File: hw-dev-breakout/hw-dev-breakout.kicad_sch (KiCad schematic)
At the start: 5 parts, among them J1 CN7, J2 CN10

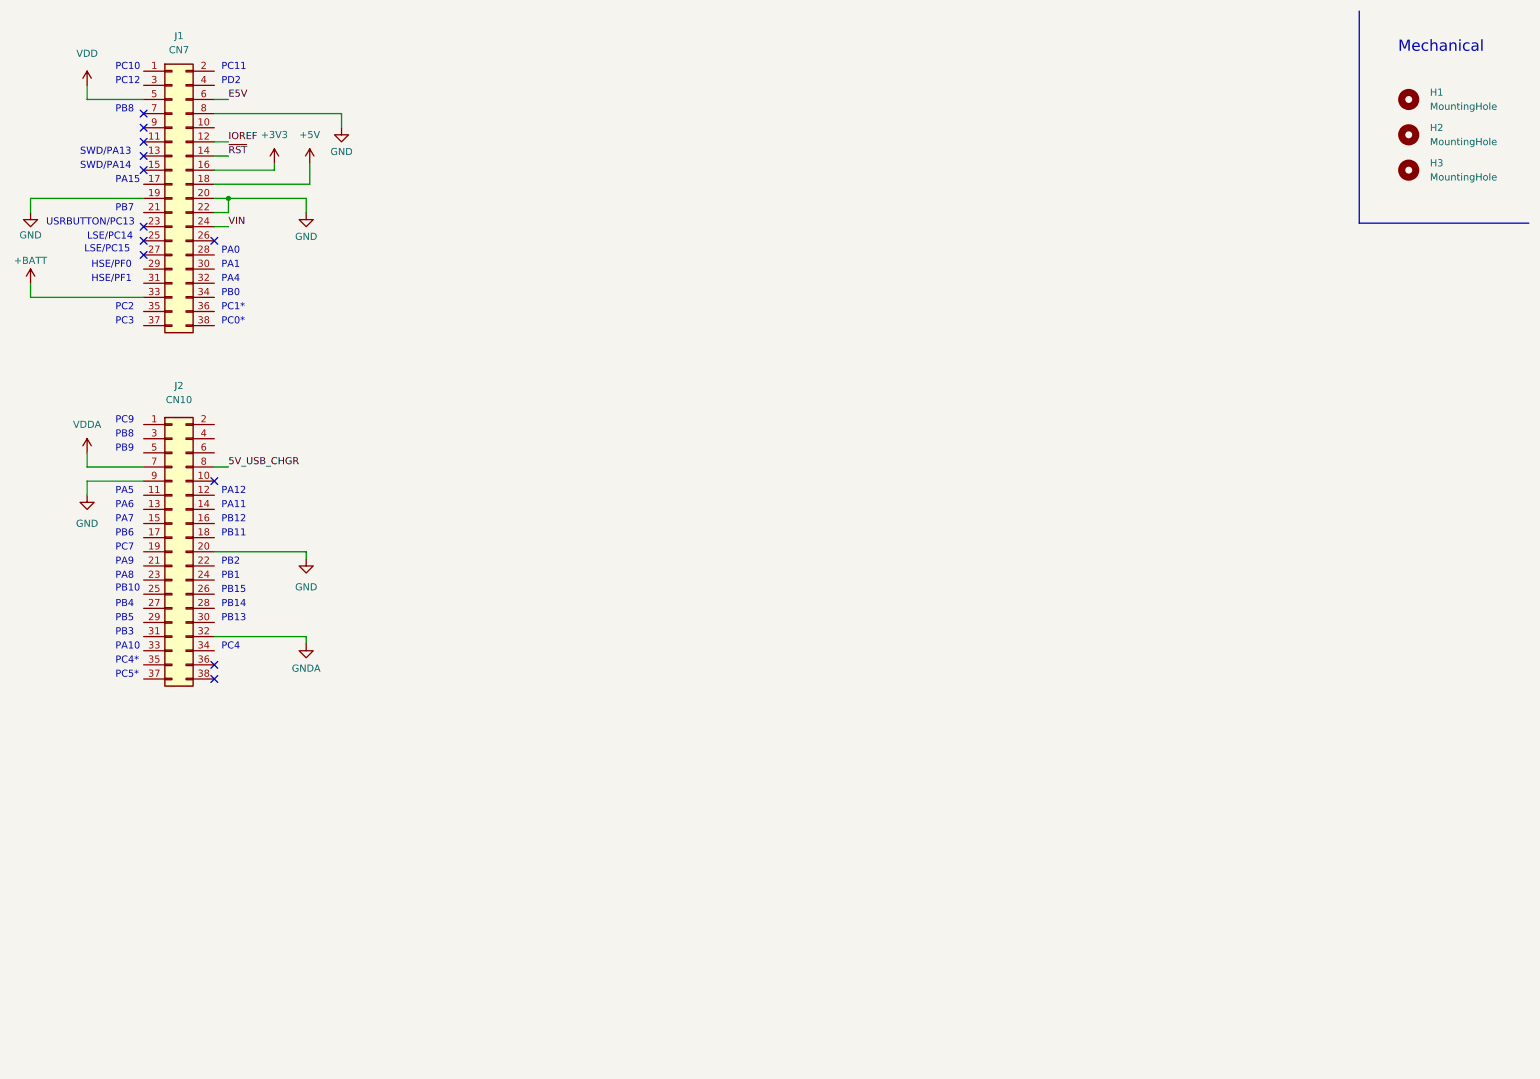
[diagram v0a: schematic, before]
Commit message: WIP: Active level shifting, too many components
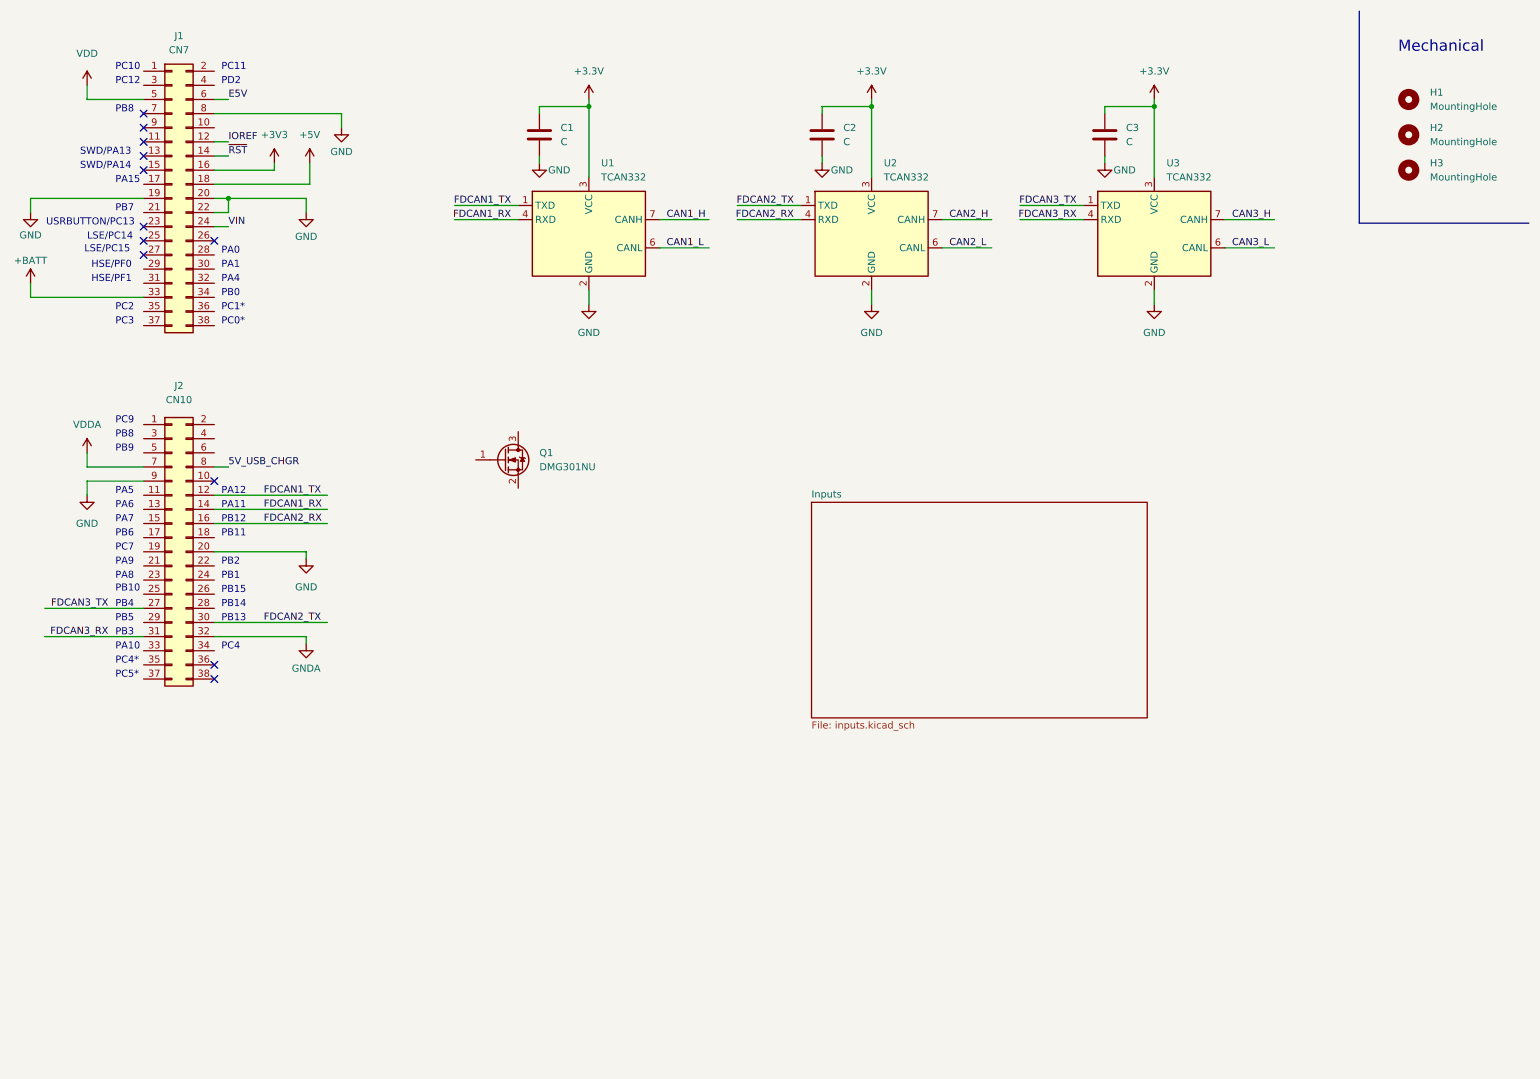
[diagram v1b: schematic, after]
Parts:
- added C1, C2, C3: C, symbol Device:C
- added Q1: DMG301NU, Package_TO_SOT_SMD:SOT-23, symbol Device:Q_NMOS_GSD
- added U1, U2, U3: TCAN332, symbol Interface_CAN_LIN:TCAN332
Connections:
- net GND: now also C1.2, C2.2, C3.2, U1.2 (GND), U2.2 (GND), U3.2 (GND)
- net FDCAN1_TX: now reaches J2.12 (Pin_12)
- net FDCAN1_TX: now also U1.1 (TXD)
- net FDCAN1_RX: now reaches J2.14 (Pin_14)
- net FDCAN1_RX: now also U1.4 (RXD)
- net FDCAN2_RX: now reaches J2.16 (Pin_16)
- net FDCAN2_RX: now also U2.4 (RXD)
- net FDCAN3_TX: now reaches J2.27 (Pin_27)
- net FDCAN3_TX: now also U3.1 (TXD)
- net FDCAN2_TX: now reaches J2.30 (Pin_30)
- net FDCAN2_TX: now also U2.1 (TXD)
- net FDCAN3_RX: now reaches J2.31 (Pin_31)
- net FDCAN3_RX: now also U3.4 (RXD)
- new net +3.3V: C1.1, C2.1, C3.1, U1.3 (VCC), U2.3 (VCC), U3.3 (VCC)
- new net CAN1_H: U1.7 (CANH)
- new net CAN1_L: U1.6 (CANL)
- new net CAN2_H: U2.7 (CANH)
- new net CAN2_L: U2.6 (CANL)
- new net CAN3_H: U3.7 (CANH)
- new net CAN3_L: U3.6 (CANL)
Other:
- added sheet Inputs (inputs.kicad_sch)

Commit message: Schematic mostly done, pre-resistor pack swap
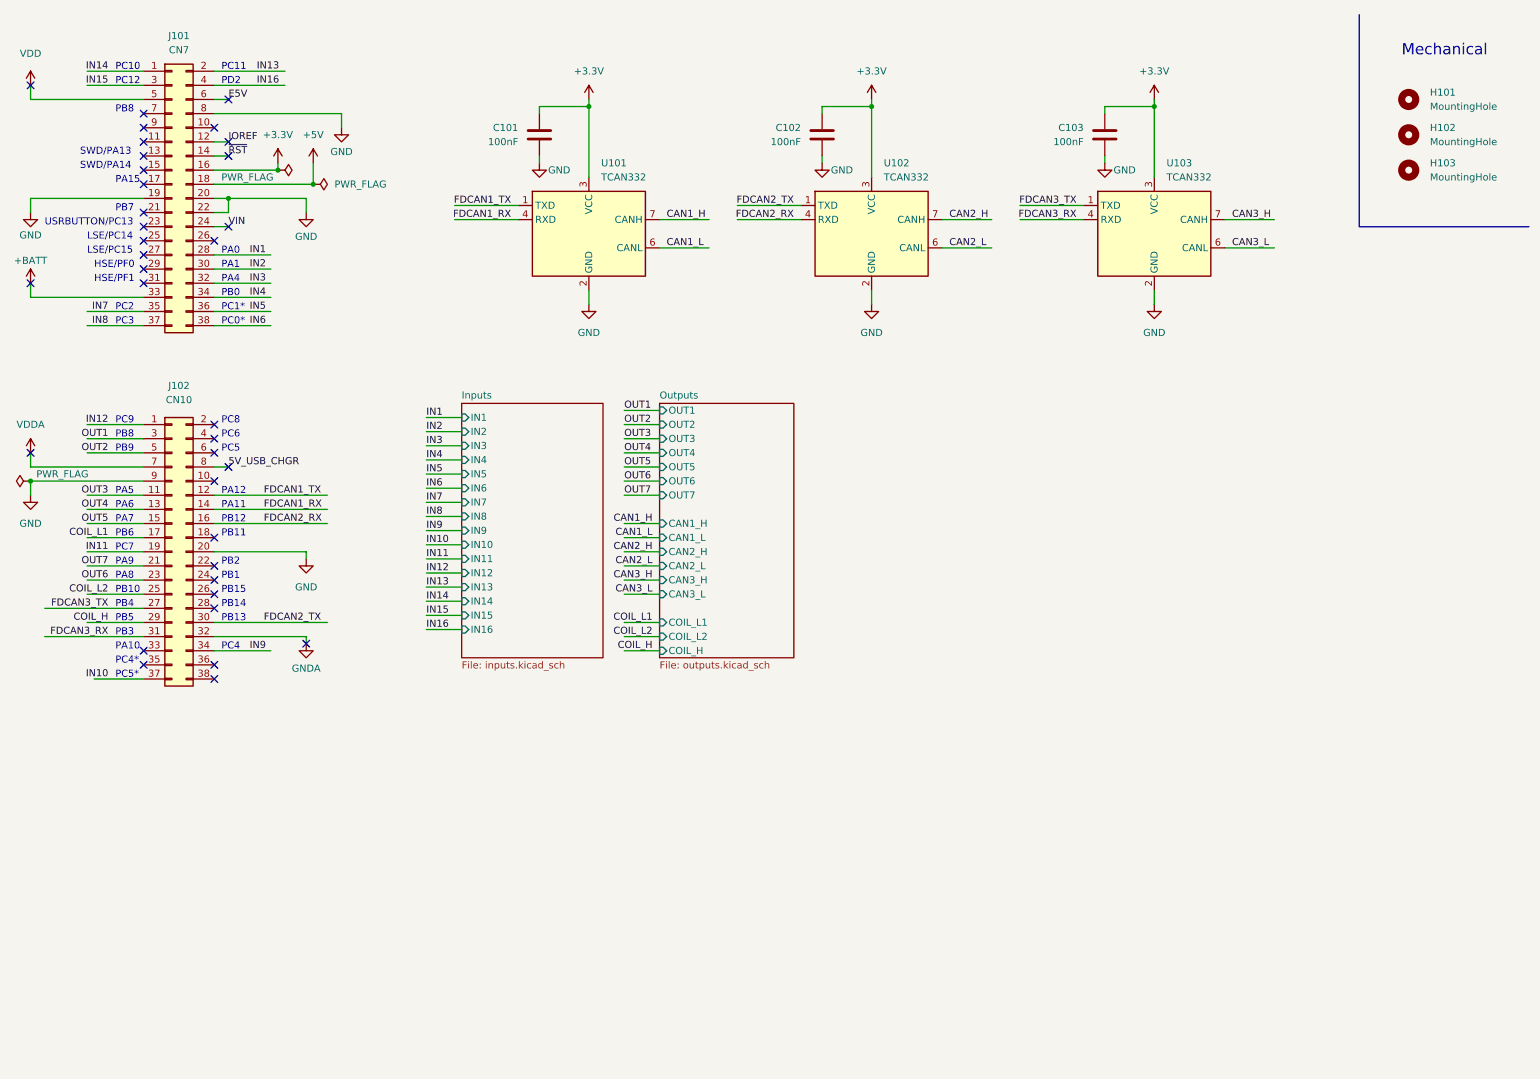
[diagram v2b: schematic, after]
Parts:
- removed Q1: DMG301NU, Package_TO_SOT_SMD:SOT-23, symbol Device:Q_NMOS_GSD
- C101: renamed from C1; value C -> 100nF; footprint (none) -> Capacitor_SMD:C_0603_1608Metric
- C102: renamed from C2; value C -> 100nF; footprint (none) -> Capacitor_SMD:C_0603_1608Metric
- C103: renamed from C3; value C -> 100nF; footprint (none) -> Capacitor_SMD:C_0603_1608Metric
- U101: renamed from U1; footprint (none) -> Package_SO:SOIC-8_3.9x4.9mm_P1.27mm
- U102: renamed from U2; footprint (none) -> Package_SO:SOIC-8_3.9x4.9mm_P1.27mm
- U103: renamed from U3; footprint (none) -> Package_SO:SOIC-8_3.9x4.9mm_P1.27mm
- renumbered H1 to H101, H2 to H102, H3 to H103, J1 to J101, J2 to J102
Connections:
- net +3V3 is gone; now on net +3.3V: J101.16 (Pin_16)
- net IN14: now reaches J101.1 (Pin_1)
- net IN13: now reaches J101.2 (Pin_2)
- net IN1: now reaches J101.28 (Pin_28)
- net IN15: now reaches J101.3 (Pin_3)
- net IN2: now reaches J101.30 (Pin_30)
- net IN3: now reaches J101.32 (Pin_32)
- net IN4: now reaches J101.34 (Pin_34)
- net IN7: now reaches J101.35 (Pin_35)
- net IN5: now reaches J101.36 (Pin_36)
- net IN8: now reaches J101.37 (Pin_37)
- net IN6: now reaches J101.38 (Pin_38)
- net IN16: now reaches J101.4 (Pin_4)
- net IN12: now reaches J102.1 (Pin_1)
- net OUT3: now reaches J102.11 (Pin_11)
- net OUT4: now reaches J102.13 (Pin_13)
- net OUT5: now reaches J102.15 (Pin_15)
- net COIL_L1: now reaches J102.17 (Pin_17)
- net IN11: now reaches J102.19 (Pin_19)
- net OUT7: now reaches J102.21 (Pin_21)
- net OUT6: now reaches J102.23 (Pin_23)
- net COIL_L2: now reaches J102.25 (Pin_25)
- net COIL_H: now reaches J102.29 (Pin_29)
- net OUT1: now reaches J102.3 (Pin_3)
- net IN9: now reaches J102.34 (Pin_34)
- net IN10: now reaches J102.37 (Pin_37)
- net OUT2: now reaches J102.5 (Pin_5)
- no-connect marks 12 -> 36
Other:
- added sheet Outputs (outputs.kicad_sch)
- sheet Inputs ports: added IN1, IN10, IN11, IN12, IN13, IN14, IN15, IN16, IN2, IN3, IN4, IN5, IN6, IN7, IN8, IN9; removed none
- note added: "PC5"
- note added: "PC6"
- note added: "PC8"

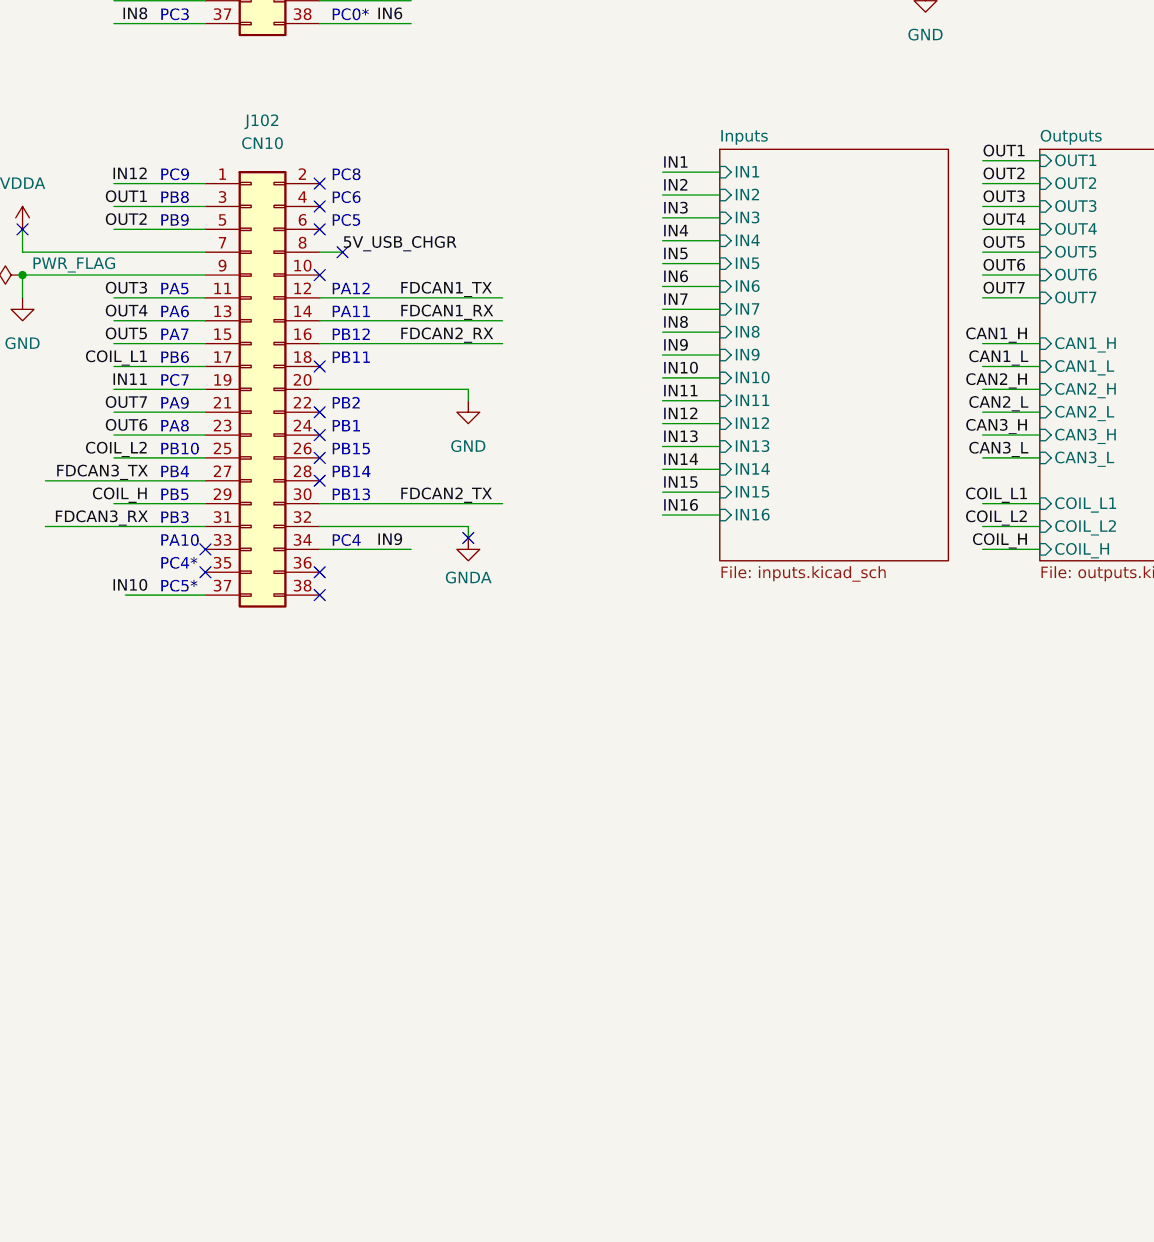
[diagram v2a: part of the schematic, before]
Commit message: Complete schematic with footprint assignments
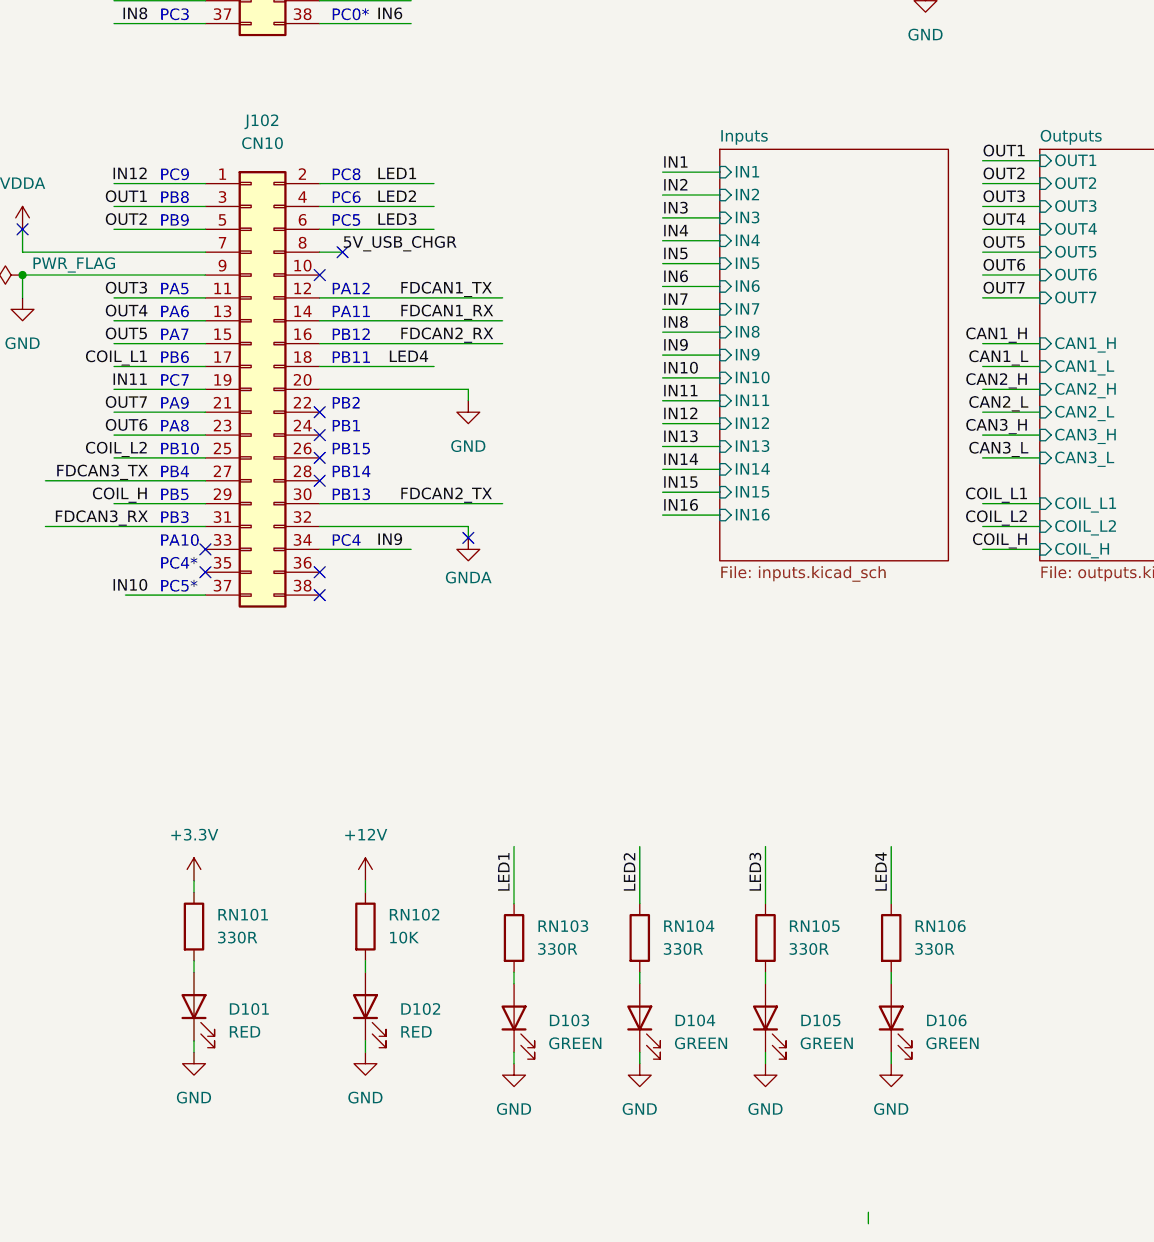
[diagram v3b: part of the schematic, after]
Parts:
- added D101, D102: RED, LED_SMD:LED_0603_1608Metric, symbol Device:LED
- added D103, D104, D105, D106: GREEN, LED_SMD:LED_0603_1608Metric, symbol Device:LED
- added RN101, RN103, RN104, RN105, RN106: 330R, Resistor_SMD:R_0603_1608Metric, symbol Device:R
- added RN102: 10K, Resistor_SMD:R_0603_1608Metric, symbol Device:R
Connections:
- net +3.3V: now also RN101.1
- net GND: now also D101.1 (K), D102.1 (K), D103.1 (K), D104.1 (K), D105.1 (K), D106.1 (K)
- net LED4: now reaches J102.18 (Pin_18)
- net LED4: now also RN106.1
- net LED1: now reaches J102.2 (Pin_2)
- net LED1: now also RN103.1
- net LED2: now reaches J102.4 (Pin_4)
- net LED2: now also RN104.1
- net LED3: now reaches J102.6 (Pin_6)
- net LED3: now also RN105.1
- new net: D103.2 (A), RN103.2
- new net: D104.2 (A), RN104.2
- new net: D105.2 (A), RN105.2
- new net: D101.2 (A), RN101.2
- new net: D106.2 (A), RN106.2
- new net: D102.2 (A), RN102.2
- new net +12V: RN102.1
- no-connect marks 36 -> 32

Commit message: pcb: Initial components placed
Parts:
- removed H101, H102, H103: MountingHole, MountingHole:MountingHole_3.2mm_M3, symbol Mechanical:MountingHole
- added SW101: SW_Push, Button_Switch_THT:SW_PUSH_6mm_H8mm, symbol Switch:SW_Push
- renumbered RN101 to R101, RN102 to R102, RN103 to R103, RN104 to R104, RN105 to R105, RN106 to R106
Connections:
- net GND: now also SW101.1
- net ~{RST}: now also SW101.2
- net +BATT: no longer names the net of J101.33 (Pin_33)
- net GNDA: no longer names the net of J102.32 (Pin_32)
- net VDD: no longer names the net of J101.5 (Pin_5)
- no-connect marks 32 -> 31
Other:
- note added: "GNDA"
- note added: "VBATT"
- note added: "VDD"
- note removed: "Mechanical"
